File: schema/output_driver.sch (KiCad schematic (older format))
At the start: 0 parts

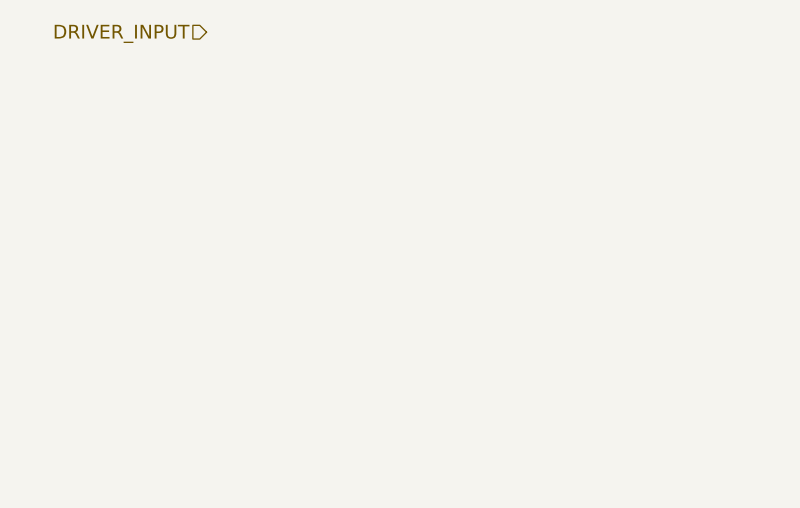
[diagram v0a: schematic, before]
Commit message: Output LED driver
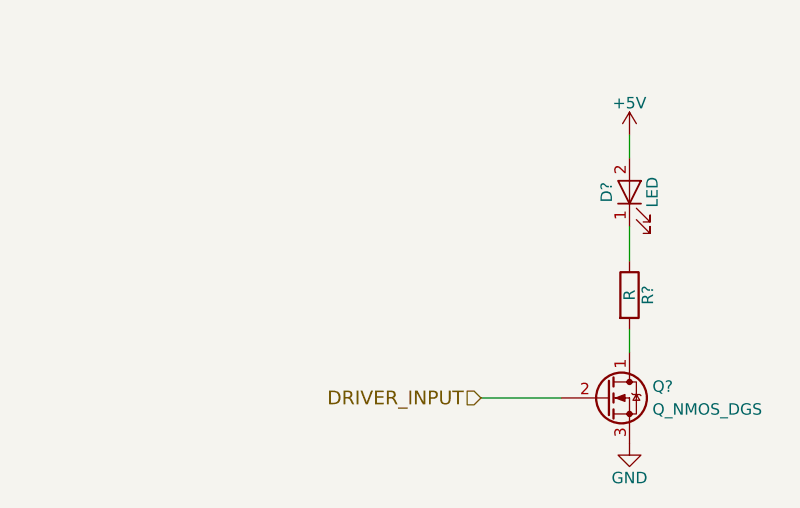
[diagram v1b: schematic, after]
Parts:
- added D?: LED, symbol LED
- added Q?: Q_NMOS_DGS, symbol Q_NMOS_DGS
- added R?: R, symbol R
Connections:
- net DRIVER_INPUT: now also Q?.2 (G)
- new net: Q?.1 (D), R?.2
- new net: D?.1 (K), R?.1
- new net +5V: D?.2 (A)
- new net GND: Q?.3 (S)
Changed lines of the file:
@@
 $Descr A4 11693 8268
 encoding utf-8
-Sheet 6 6
+Sheet 5 6
 Title ""
 Date ""
@@
 Comment4 ""
 $EndDescr
-Text HLabel 3900 2500 0    60   Input ~ 0
+Text HLabel 5100 4100 0    60   Input ~ 0
 DRIVER_INPUT
+$Comp
+L Q_NMOS_DGS Q?
+U 1 1 5910A46B
+P 5650 4100
+F 0 "Q?" H 5850 4150 50  0000 L CNN
+F 1 "Q_NMOS_DGS" H 5850 4050 50  0000 L CNN
+F 2 "" H 5850 4200 50  0000 C CNN
+F 3 "" H 5650 4100 50  0000 C CNN
+	1    5650 4100
+	1    0    0    -1
+$EndComp
+$Comp
+L LED D?
+U 1 1 5910A491
+P 5750 3200
+F 0 "D?" H 5750 3300 50  0000 C CNN
+F 1 "LED" H 5750 3100 50  0000 C CNN
+F 2 "" H 5750 3200 50  0000 C CNN
+F 3 "" H 5750 3200 50  0000 C CNN
+	1    5750 3200
+	0    -1   -1   0
+$EndComp
+Wire Wire Line
+	5750 3800 5750 3900
+Wire Wire Line
+	5750 2950 5750 3050
+$Comp
+L +5V #PWR?
+U 1 1 5910A522
+P 5750 2950
+F 0 "#PWR?" H 5750 2800 50  0001 C CNN
+F 1 "+5V" H 5750 3090 50  0000 C CNN
+F 2 "" H 5750 2950 50  0000 C CNN
+F 3 "" H 5750 2950 50  0000 C CNN
+	1    5750 2950
+	1    0    0    -1
+$EndComp
+$Comp
+L GND #PWR?
+U 1 1 5910A53C
+P 5750 4300
+F 0 "#PWR?" H 5750 4050 50  0001 C CNN
+F 1 "GND" H 5750 4150 50  0000 C CNN
+F 2 "" H 5750 4300 50  0000 C CNN
+F 3 "" H 5750 4300 50  0000 C CNN
+	1    5750 4300
+	1    0    0    -1
+$EndComp
+$Comp
+L R R?
+U 1 1 5910A571
+P 5750 3650
+F 0 "R?" V 5830 3650 50  0000 C CNN
+F 1 "R" V 5750 3650 50  0000 C CNN
+F 2 "" V 5680 3650 50  0000 C CNN
+F 3 "" H 5750 3650 50  0000 C CNN
+	1    5750 3650
+	1    0    0    -1
+$EndComp
+Wire Wire Line
+	5750 3350 5750 3500
+Wire Wire Line
+	5450 4100 5100 4100
 $EndSCHEMATC
